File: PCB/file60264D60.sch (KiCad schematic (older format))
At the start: 44 parts, among them J6 10129379-905001BLF, J8 PJ-102AH, Q1 FDD6685, Q2 2N7002K, SW0 B3F-1055, U1 LMZ22005TZ_NOPB

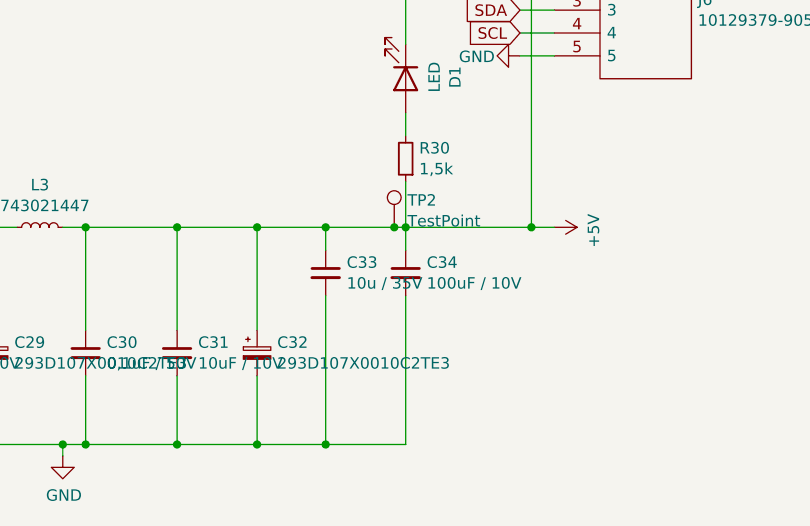
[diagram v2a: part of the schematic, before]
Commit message: Refactored JLC Part Numbers. And replaced 100uF capacitors with 1206 sized parts.
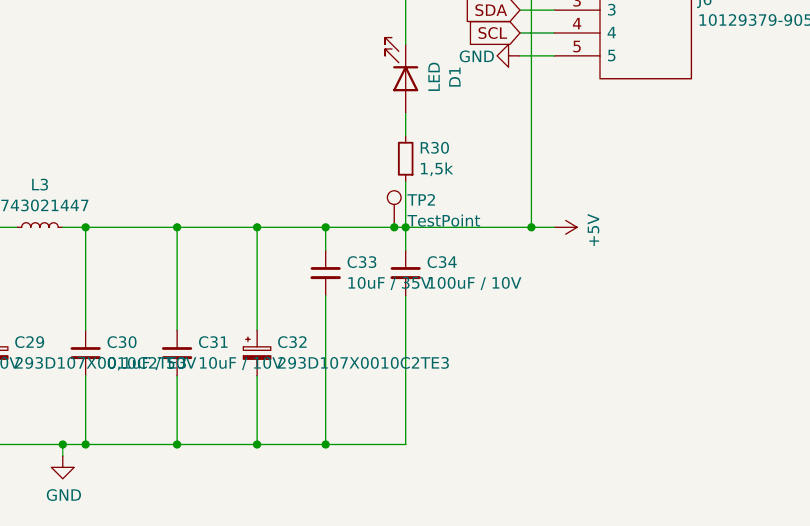
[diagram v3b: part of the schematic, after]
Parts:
- C12, C19, C21, C23, C25, C27, C30: LCSC C62912 -> C49678
- C14, C20, C24: LCSC (none) -> C15850; Manufacturer_Part_Number CL21A106KBYQNNE -> CL21A106KAYNNNE; Mouser Part Number 187-CL21A106KBYQNNE -> 187-CL21A106KAYNNNE
- C18: LCSC C167035 -> (none)
- C22: LCSC C130385 -> (none)
- C26: LCSC (none) -> C13967; Manufacturer_Part_Number CL21B474KOFNNNE -> CL21B474KBFNNNE; Mouser Part Number 187-CL21B474KOFNNNE -> 187-CL21B474KBFNNNE
- C28, C31: LCSC C91245 -> C15850
- C29, C32: LCSC C136005 -> (none)
- C33: value 10u / 35V -> 10uF / 35V; LCSC (none) -> C15850; Manufacturer_Part_Number CL21A106KBYQNNE -> CL21A106KAYNNNE; Mouser Part Number 187-CL21A106KBYQNNE -> 187-CL21A106KAYNNNE
- C34: footprint Capacitor_SMD:C_0805_2012Metric_Pad1.15x1.40mm_HandSolder -> Capacitor_SMD:C_1206_3216Metric_Pad1.42x1.75mm_HandSolder; LCSC C307523 -> C84455; Manufacturer_Name Samsung Electro-Mechanics -> Murata Electronics; Manufacturer_Part_Number CL21A106KPFNNNG -> GRM32ER61A107ME20L; Mouser Part Number 187-CL21A106KPFNNNG -> 81-GRM32ER61A107ME0L
- R60: LCSC C17782 -> C23220
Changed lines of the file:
@@
 F 2 "Capacitor_SMD:C_0805_2012Metric_Pad1.15x1.40mm_HandSolder" H 8250 1250 50  0001 C CNN
 F 3 "~" H 8250 1250 50  0001 C CNN
-F 4 "C62912" H 8250 1250 50  0001 C CNN "LCSC"
+F 4 "C49678" H 8250 1250 50  0001 C CNN "LCSC"
 F 5 "Samsung Electro-Mechanics" H 8250 1250 50  0001 C CNN "Manufacturer_Name"
 F 6 "CL21B104KBCSFNC" H 8250 1250 50  0001 C CNN "Manufacturer_Part_Number"
@@
 F 3 "~" H 8550 1250 50  0001 C CNN
 F 4 "Samsung Electro-Mechanics" H 8550 1250 50  0001 C CNN "Manufacturer_Name"
-F 5 "CL21A106KBYQNNE" H 8550 1250 50  0001 C CNN "Manufacturer_Part_Number"
-F 6 "187-CL21A106KBYQNNE" H 8550 1250 50  0001 C CNN "Mouser Part Number"
+F 5 "CL21A106KAYNNNE" H 8550 1250 50  0001 C CNN "Manufacturer_Part_Number"
+F 6 "187-CL21A106KAYNNNE" H 8550 1250 50  0001 C CNN "Mouser Part Number"
+F 7 "C15850" H 8550 1250 50  0001 C CNN "LCSC"
 	1    8550 1250
 	1    0    0    -1
@@
 F 8 "Vishay" H 7350 950 50  0001 L CNN "Manufacturer_Name"
 F 9 "293D226X9035D2TE3" H 7350 850 50  0001 L CNN "Manufacturer_Part_Number"
-F 10 "C167035" H 7000 1500 50  0001 C CNN "LCSC"
+F 10 "" H 7000 1500 50  0001 C CNN "LCSC"
 	1    7000 1500
 	1    0    0    -1
@@
 F 2 "Capacitor_SMD:C_0805_2012Metric_Pad1.15x1.40mm_HandSolder" H 6300 1450 50  0001 C CNN
 F 3 "~" H 6300 1450 50  0001 C CNN
-F 4 "C62912" H 6300 1450 50  0001 C CNN "LCSC"
+F 4 "C49678" H 6300 1450 50  0001 C CNN "LCSC"
 F 5 "Samsung Electro-Mechanics" H 6300 1450 50  0001 C CNN "Manufacturer_Name"
 F 6 "CL21B104KBCSFNC" H 6300 1450 50  0001 C CNN "Manufacturer_Part_Number"
@@
 F 2 "Capacitor_SMD:C_0805_2012Metric_Pad1.15x1.40mm_HandSolder" H 3150 2850 50  0001 C CNN
 F 3 "~" H 3150 2850 50  0001 C CNN
-F 4 "C62912" H 3150 2850 50  0001 C CNN "LCSC"
+F 4 "C49678" H 3150 2850 50  0001 C CNN "LCSC"
 F 5 "Samsung Electro-Mechanics" H 3150 2850 50  0001 C CNN "Manufacturer_Name"
 F 6 "CL21B104KBCSFNC" H 3150 2850 50  0001 C CNN "Manufacturer_Part_Number"
@@
 F 3 "~" H 3150 2200 50  0001 C CNN
 F 4 "Samsung Electro-Mechanics" H 3150 2200 50  0001 C CNN "Manufacturer_Name"
-F 5 "CL21A106KBYQNNE" H 3150 2200 50  0001 C CNN "Manufacturer_Part_Number"
-F 6 "187-CL21A106KBYQNNE" H 3150 2200 50  0001 C CNN "Mouser Part Number"
+F 5 "CL21A106KAYNNNE" H 3150 2200 50  0001 C CNN "Manufacturer_Part_Number"
+F 6 "187-CL21A106KAYNNNE" H 3150 2200 50  0001 C CNN "Mouser Part Number"
+F 7 "C15850" H 3150 2200 50  0001 C CNN "LCSC"
 	1    3150 2200
 	1    0    0    -1
@@
 F 2 "Capacitor_SMD:C_0805_2012Metric_Pad1.15x1.40mm_HandSolder" H 1800 2150 50  0001 C CNN
 F 3 "~" H 1800 2150 50  0001 C CNN
-F 4 "C62912" H 1800 2150 50  0001 C CNN "LCSC"
+F 4 "C49678" H 1800 2150 50  0001 C CNN "LCSC"
 F 5 "Samsung Electro-Mechanics" H 1800 2150 50  0001 C CNN "Manufacturer_Name"
 F 6 "CL21B104KBCSFNC" H 1800 2150 50  0001 C CNN "Manufacturer_Part_Number"
@@
 F 3 "~" H 4450 2050 50  0001 C CNN
 F 4 "Samsung Electro-Mechanics" H 4450 2050 50  0001 C CNN "Manufacturer_Name"
-F 5 "CL21A106KBYQNNE" H 4450 2050 50  0001 C CNN "Manufacturer_Part_Number"
-F 6 "187-CL21A106KBYQNNE" H 4450 2050 50  0001 C CNN "Mouser Part Number"
+F 5 "CL21A106KAYNNNE" H 4450 2050 50  0001 C CNN "Manufacturer_Part_Number"
+F 6 "187-CL21A106KAYNNNE" H 4450 2050 50  0001 C CNN "Mouser Part Number"
+F 7 "C15850" H 4450 2050 50  0001 C CNN "LCSC"
 	1    4450 2050
 	1    0    0    -1
@@
 F 2 "Capacitor_SMD:C_0805_2012Metric_Pad1.15x1.40mm_HandSolder" H 4450 5200 50  0001 C CNN
 F 3 "~" H 4450 5200 50  0001 C CNN
-F 4 "C62912" H 4450 5200 50  0001 C CNN "LCSC"
+F 4 "C49678" H 4450 5200 50  0001 C CNN "LCSC"
 F 5 "Samsung Electro-Mechanics" H 4450 5200 50  0001 C CNN "Manufacturer_Name"
 F 6 "CL21B104KBCSFNC" H 4450 5200 50  0001 C CNN "Manufacturer_Part_Number"
@@
 F 2 "Capacitor_SMD:C_0805_2012Metric_Pad1.15x1.40mm_HandSolder" H 7600 5300 50  0001 C CNN
 F 3 "~" H 7600 5300 50  0001 C CNN
-F 4 "C62912" H 7600 5300 50  0001 C CNN "LCSC"
+F 4 "C49678" H 7600 5300 50  0001 C CNN "LCSC"
 F 5 "Samsung Electro-Mechanics" H 7600 5300 50  0001 C CNN "Manufacturer_Name"
 F 6 "CL21B104KBCSFNC" H 7600 5300 50  0001 C CNN "Manufacturer_Part_Number"
@@
 F 2 "Capacitor_SMD:C_0805_2012Metric_Pad1.15x1.40mm_HandSolder" H 8000 5300 50  0001 C CNN
 F 3 "~" H 8000 5300 50  0001 C CNN
-F 4 "C91245" H 8000 5300 50  0001 C CNN "LCSC"
+F 4 "C15850" H 8000 5300 50  0001 C CNN "LCSC"
 F 5 "Samsung Electro-Mechanics" H 8000 5300 50  0001 C CNN "Manufacturer_Name"
 F 6 "CL21A106MPFNNNE" H 8000 5300 50  0001 C CNN "Manufacturer_Part_Number"
@@
 F 2 "Capacitor_SMD:C_0805_2012Metric_Pad1.15x1.40mm_HandSolder" H 6450 5300 50  0001 C CNN
 F 3 "~" H 6450 5300 50  0001 C CNN
-F 4 "C62912" H 6450 5300 50  0001 C CNN "LCSC"
+F 4 "C49678" H 6450 5300 50  0001 C CNN "LCSC"
 F 5 "Samsung Electro-Mechanics" H 6450 5300 50  0001 C CNN "Manufacturer_Name"
 F 6 "CL21B104KBCSFNC" H 6450 5300 50  0001 C CNN "Manufacturer_Part_Number"
@@
 F 2 "Capacitor_SMD:C_0805_2012Metric_Pad1.15x1.40mm_HandSolder" H 6850 5300 50  0001 C CNN
 F 3 "~" H 6850 5300 50  0001 C CNN
-F 4 "C91245" H 6850 5300 50  0001 C CNN "LCSC"
+F 4 "C15850" H 6850 5300 50  0001 C CNN "LCSC"
 F 5 "Samsung Electro-Mechanics" H 6850 5300 50  0001 C CNN "Manufacturer_Name"
 F 6 "CL21A106MPFNNNE" H 6850 5300 50  0001 C CNN "Manufacturer_Part_Number"
@@
 F 8 "Vishay" H 7550 4750 50  0001 L CNN "Manufacturer_Name"
 F 9 "293D107X0010C2TE3" H 7550 4650 50  0001 L CNN "Manufacturer_Part_Number"
-F 10 "C136005" H 7200 5300 50  0001 C CNN "LCSC"
+F 10 "" H 7200 5300 50  0001 C CNN "LCSC"
 	1    7200 5300
 	1    0    0    -1
@@
 P 8650 4950
 F 0 "C33" H 8742 4996 50  0000 L CNN
-F 1 "10u / 35V" H 8742 4905 50  0000 L CNN
+F 1 "10uF / 35V" H 8742 4905 50  0000 L CNN
 F 2 "Capacitor_SMD:C_0805_2012Metric_Pad1.15x1.40mm_HandSolder" H 8650 4950 50  0001 C CNN
 F 3 "~" H 8650 4950 50  0001 C CNN
 F 4 "Samsung Electro-Mechanics" H 8650 4950 50  0001 C CNN "Manufacturer_Name"
-F 5 "CL21A106KBYQNNE" H 8650 4950 50  0001 C CNN "Manufacturer_Part_Number"
-F 6 "187-CL21A106KBYQNNE" H 8650 4950 50  0001 C CNN "Mouser Part Number"
+F 5 "CL21A106KAYNNNE" H 8650 4950 50  0001 C CNN "Manufacturer_Part_Number"
+F 6 "187-CL21A106KAYNNNE" H 8650 4950 50  0001 C CNN "Mouser Part Number"
+F 7 "C15850" H 8650 4950 50  0001 C CNN "LCSC"
 	1    8650 4950
 	1    0    0    -1
@@
 F 0 "C34" H 9092 4996 50  0000 L CNN
 F 1 "100uF / 10V" H 9092 4905 50  0000 L CNN
-F 2 "Capacitor_SMD:C_0805_2012Metric_Pad1.15x1.40mm_HandSolder" H 9000 4950 50  0001 C CNN
+F 2 "Capacitor_SMD:C_1206_3216Metric_Pad1.42x1.75mm_HandSolder" H 9000 4950 50  0001 C CNN
 F 3 "~" H 9000 4950 50  0001 C CNN
-F 4 "C307523" H 9000 4950 50  0001 C CNN "LCSC"
-F 5 "Samsung Electro-Mechanics" H 9000 4950 50  0001 C CNN "Manufacturer_Name"
-F 6 "CL21A106KPFNNNG" H 9000 4950 50  0001 C CNN "Manufacturer_Part_Number"
-F 7 "187-CL21A106KPFNNNG" H 9000 4950 50  0001 C CNN "Mouser Part Number"
+F 4 "C84455" H 9000 4950 50  0001 C CNN "LCSC"
+F 5 "Murata Electronics" H 9000 4950 50  0001 C CNN "Manufacturer_Name"
+F 6 "GRM32ER61A107ME20L" H 9000 4950 50  0001 C CNN "Manufacturer_Part_Number"
+F 7 "81-GRM32ER61A107ME0L" H 9000 4950 50  0001 C CNN "Mouser Part Number"
 	1    9000 4950
 	1    0    0    -1
@@
 F 8 "Vishay" H 8700 4750 50  0001 L CNN "Manufacturer_Name"
 F 9 "293D107X0010C2TE3" H 8700 4650 50  0001 L CNN "Manufacturer_Part_Number"
-F 10 "C136005" H 8350 5300 50  0001 C CNN "LCSC"
+F 10 "" H 8350 5300 50  0001 C CNN "LCSC"
 	1    8350 5300
 	1    0    0    -1
@@
 F 8 "Vishay" H 4500 4650 50  0001 L CNN "Manufacturer_Name"
 F 9 "293D476X0016D2TE3" H 4500 4550 50  0001 L CNN "Manufacturer_Part_Number"
-F 10 "C130385" H 4150 5200 50  0001 C CNN "LCSC"
+F 10 "" H 4150 5200 50  0001 C CNN "LCSC"
 	1    4150 5200
 	1    0    0    -1
@@
 F 2 "Resistor_SMD:R_0805_2012Metric_Pad1.15x1.40mm_HandSolder" H 5350 5200 50  0001 C CNN
 F 3 "~" H 5350 5200 50  0001 C CNN
-F 4 "C17782" H 5350 5200 50  0001 C CNN "LCSC"
+F 4 "C23220" H 5350 5200 50  0001 C CNN "LCSC"
 F 5 "Vishay" H 5350 5200 50  0001 C CNN "Manufacturer_Name"
 F 6 "CRCW0805620RFKEA" H 5350 5200 50  0001 C CNN "Manufacturer_Part_Number"
@@
 F 3 "~" H 5650 5200 50  0001 C CNN
 F 4 "Samsung Electro-Mechanics" H 5650 5200 50  0001 C CNN "Manufacturer_Name"
-F 5 "CL21B474KOFNNNE" H 5650 5200 50  0001 C CNN "Manufacturer_Part_Number"
-F 6 "187-CL21B474KOFNNNE" H 5650 5200 50  0001 C CNN "Mouser Part Number"
+F 5 "CL21B474KBFNNNE" H 5650 5200 50  0001 C CNN "Manufacturer_Part_Number"
+F 6 "187-CL21B474KBFNNNE" H 5650 5200 50  0001 C CNN "Mouser Part Number"
+F 7 "C13967" H 5650 5200 50  0001 C CNN "LCSC"
 	1    5650 5200
 	1    0    0    -1
